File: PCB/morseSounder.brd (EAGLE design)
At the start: 56.6 x 82.7 mm, 81 parts, among them IC1 LM386M-1, IC5 LM321MF, J1 AVR_SPI_PRG_6PTH, J2 POWERPOLE_POWER25A_HORIZONTAL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, J3 POWER_JACKPTH, Q1 MMBT3904, Q2 MMBT3904, Q3 MMBT3904, Q4 2.5A/30V/105mΩ, Q5 MMBT3904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

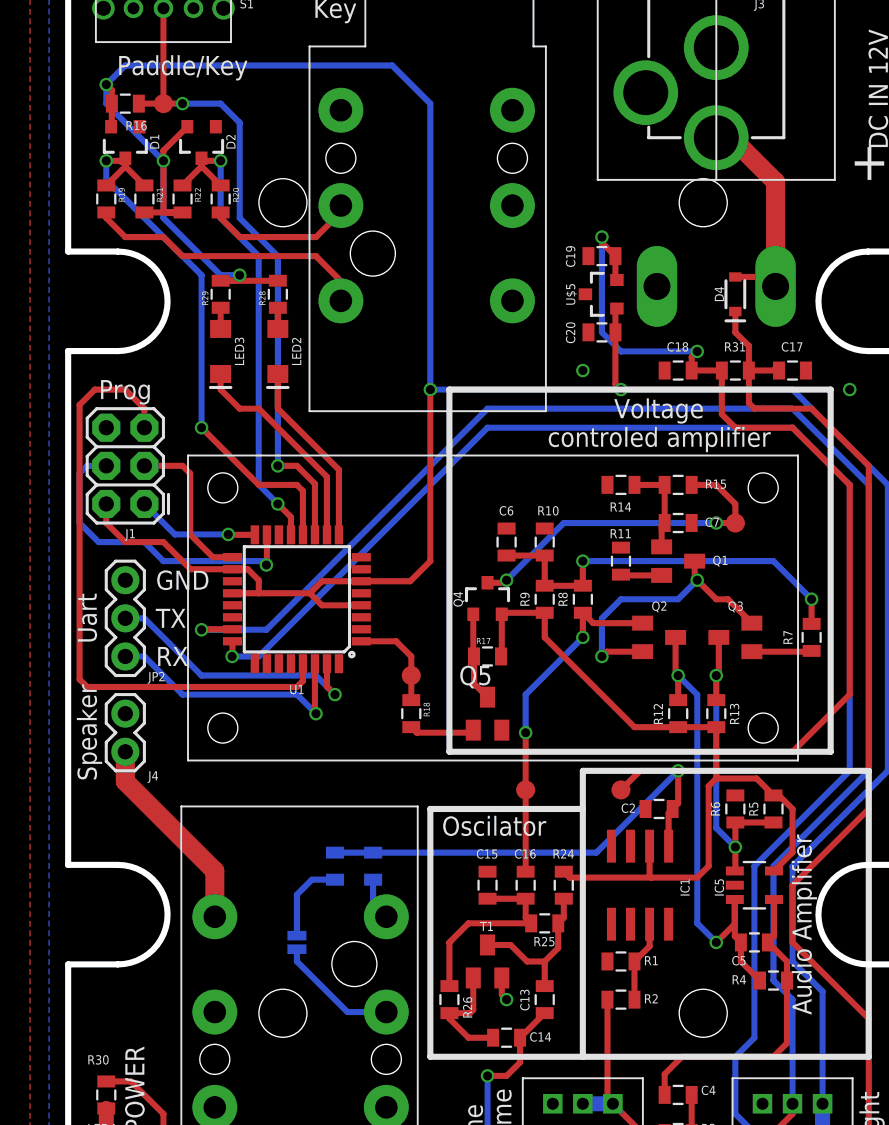
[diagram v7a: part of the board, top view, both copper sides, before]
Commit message: Added some decoupling capacitors and tidied silk screen
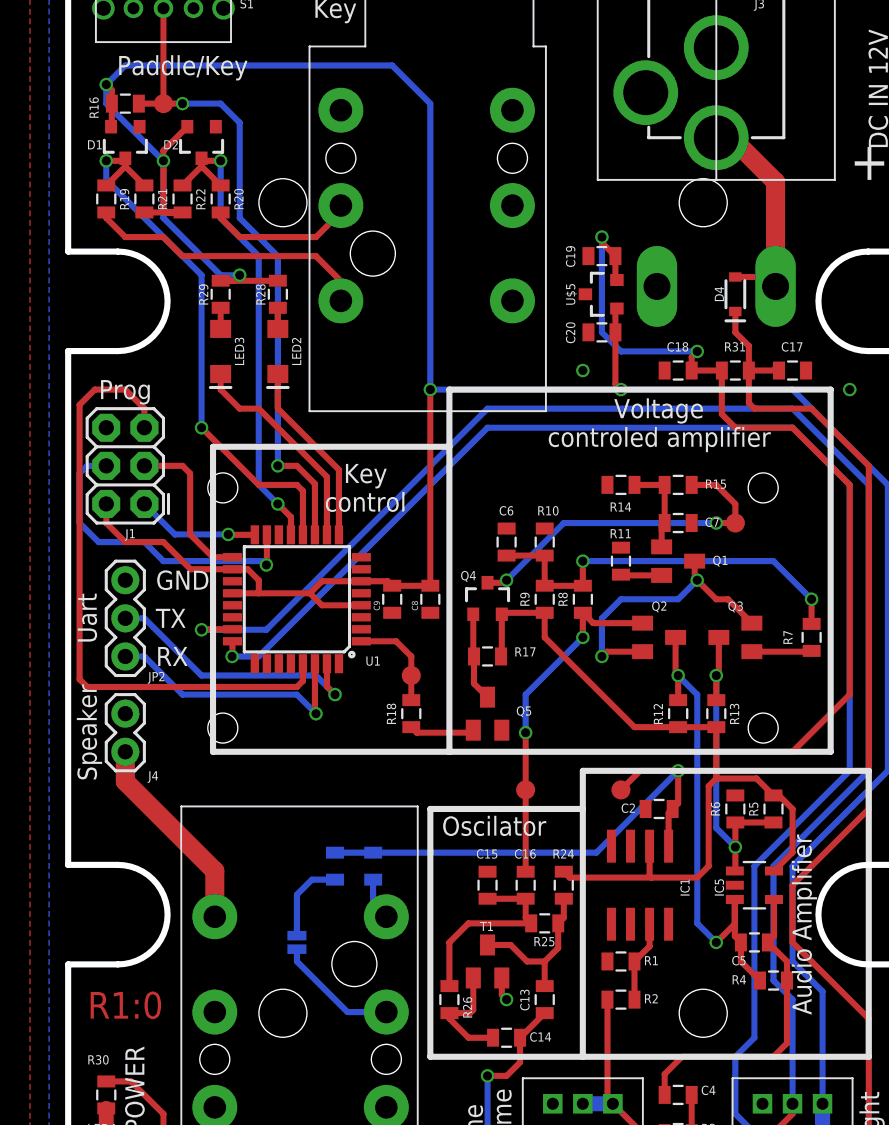
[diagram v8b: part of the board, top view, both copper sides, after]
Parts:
- added C8: 100n, SparkFun:0805
- added C9: 10n, SparkFun:0805
- added U$7: LOGO_SUWSLOGO_LARGE, morseSounder:LOGO_SUWS
- flipped U$4 to the bottom
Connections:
- net AVR_VCC: now also C8.2, C9.2
- net GND: now also C8.1, C9.1
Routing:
- net AVR_VCC: track 208.7 -> 209.9 mm
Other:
- board text added: "Key control"
- board text added: "R1:0"
- board text added: "www.SUWS.org.uk"
